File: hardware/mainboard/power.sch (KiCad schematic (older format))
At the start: 12 parts, among them U1 LM4040DBZ-10, U2 LM1117-3.3

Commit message: First pass layout & component selection for mainboard
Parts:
- C1, C4: footprint Capacitor_SMD:C_0805_2012Metric_Pad1.15x1.40mm_HandSolder -> Capacitor_SMD:C_0603_1608Metric_Pad1.05x0.95mm_HandSolder; finalized no -> yes
- D1, D2, FB1, FB2, FB3, U1: finalized no -> yes
- R1: footprint Resistor_SMD:R_1206_3216Metric_Pad1.42x1.75mm_HandSolder -> Resistor_SMD:R_0603_1608Metric_Pad1.05x0.95mm_HandSolder; Reqs (none) -> 1%; mpn ERA8AEB222V -> ERA-3AED222V
- U2: finalized no -> yes; mpn (none) -> LM1117IMP-3.3/NOPB
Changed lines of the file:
@@
 F 2 "Diode_SMD:D_SOD-123" H 2250 1100 50  0001 C CNN
 F 3 "~" H 2250 1100 50  0001 C CNN
-F 4 "no" H 2250 1100 50  0001 C CNN "finalized"
+F 4 "yes" H 2250 1100 50  0001 C CNN "finalized"
 F 5 "MF-DIO-SOD123-1N4148" H 2250 1100 50  0001 C CNN "mpn"
 	1    2250 1100
@@
 F 2 "Diode_SMD:D_SOD-123" H 2250 1600 50  0001 C CNN
 F 3 "~" H 2250 1600 50  0001 C CNN
-F 4 "no" H 2250 1600 50  0001 C CNN "finalized"
+F 4 "yes" H 2250 1600 50  0001 C CNN "finalized"
 F 5 "MF-DIO-SOD123-1N4148" H 2250 1600 50  0001 C CNN "mpn"
 	1    2250 1600
@@
 F 2 "Package_TO_SOT_SMD:SOT-223-3_TabPin2" H 4650 1200 50  0001 C CNN
 F 3 "http://www.ti.com/lit/ds/symlink/lm1117.pdf" H 4650 1200 50  0001 C CNN
-F 4 "no" H 4650 1200 50  0001 C CNN "finalized"
+F 4 "yes" H 4650 1200 50  0001 C CNN "finalized"
+F 5 "LM1117IMP-3.3/NOPB" H 4650 1200 50  0001 C CNN "mpn"
 	1    4650 1200
 	1    0    0    -1
@@
 F 0 "C4" H 5715 1396 50  0000 L CNN
 F 1 "0.1uF" H 5715 1305 50  0000 L CNN
-F 2 "Capacitor_SMD:C_0805_2012Metric_Pad1.15x1.40mm_HandSolder" H 5638 1200 50  0001 C CNN
+F 2 "Capacitor_SMD:C_0603_1608Metric_Pad1.05x0.95mm_HandSolder" H 5638 1200 50  0001 C CNN
 F 3 "~" H 5600 1350 50  0001 C CNN
-F 4 "no" H 5600 1350 50  0001 C CNN "finalized"
+F 4 "yes" H 5600 1350 50  0001 C CNN "finalized"
 F 5 "MF-CAP-0603-0.1uF" H 5600 1350 50  0001 C CNN "mpn"
 	1    5600 1350
@@
 F 3 "~" H 5950 1100 50  0001 C CNN
 F 4 "710-742792664" H 5950 1100 50  0001 C CNN "mpn"
-F 5 "no" H 5950 1100 50  0001 C CNN "finalized"
+F 5 "yes" H 5950 1100 50  0001 C CNN "finalized"
 	1    5950 1100
 	-1   0    0    1
@@
 F 3 "~" H 1800 1600 50  0001 C CNN
 F 4 "710-742792664" H 1800 1600 50  0001 C CNN "mpn"
-F 5 "no" H 1800 1600 50  0001 C CNN "finalized"
+F 5 "yes" H 1800 1600 50  0001 C CNN "finalized"
 	1    1800 1600
 	0    -1   -1   0
@@
 F 2 "Package_TO_SOT_SMD:SOT-23" H 2200 3100 50  0001 C CIN
 F 3 "http://www.ti.com/lit/ds/symlink/lm4040-n.pdf" H 2200 3300 50  0001 C CIN
-F 4 "no" H 2200 3300 50  0001 C CNN "finalized"
+F 4 "yes" H 2200 3300 50  0001 C CNN "finalized"
 F 5 "LM4040DIM3-10.0/NOPB" H 2200 3300 50  0001 C CNN "mpn"
 	1    2200 3300
@@
 F 0 "R1" H 2268 2846 50  0000 L CNN
 F 1 "2.2k" H 2268 2755 50  0000 L CNN
-F 2 "Resistor_SMD:R_1206_3216Metric_Pad1.42x1.75mm_HandSolder" V 2240 2790 50  0001 C CNN
+F 2 "Resistor_SMD:R_0603_1608Metric_Pad1.05x0.95mm_HandSolder" V 2240 2790 50  0001 C CNN
 F 3 "~" H 2200 2800 50  0001 C CNN
 F 4 "no" H 2200 2800 50  0001 C CNN "finalized"
-F 5 "ERA8AEB222V" H 2200 2800 50  0001 C CNN "mpn"
+F 5 "ERA-3AED222V" H 2200 2800 50  0001 C CNN "mpn"
+F 6 "1%" H 2200 2800 50  0001 C CNN "Reqs"
 	1    2200 2800
 	1    0    0    -1
@@
 F 0 "C1" H 2665 3346 50  0000 L CNN
 F 1 "0.1uF" H 2665 3255 50  0000 L CNN
-F 2 "Capacitor_SMD:C_0805_2012Metric_Pad1.15x1.40mm_HandSolder" H 2588 3150 50  0001 C CNN
+F 2 "Capacitor_SMD:C_0603_1608Metric_Pad1.05x0.95mm_HandSolder" H 2588 3150 50  0001 C CNN
 F 3 "~" H 2550 3300 50  0001 C CNN
-F 4 "no" H 2550 3300 50  0001 C CNN "finalized"
+F 4 "yes" H 2550 3300 50  0001 C CNN "finalized"
 F 5 "MF-CAP-0603-0.1uF" H 2550 3300 50  0001 C CNN "mpn"
 	1    2550 3300
@@
 F 3 "~" H 1800 1100 50  0001 C CNN
 F 4 "710-742792664" H 1800 1100 50  0001 C CNN "mpn"
-F 5 "no" H 1800 1100 50  0001 C CNN "finalized"
+F 5 "yes" H 1800 1100 50  0001 C CNN "finalized"
 	1    1800 1100
 	0    -1   -1   0

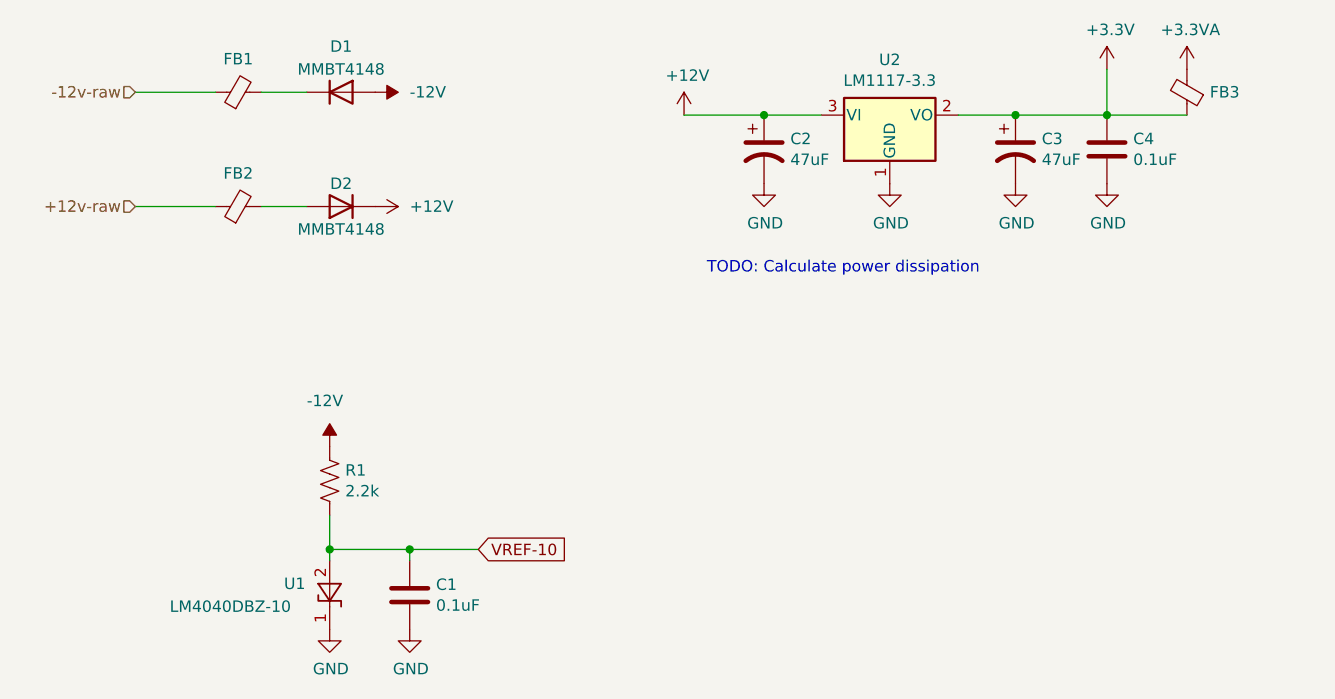
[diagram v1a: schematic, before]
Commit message: Refine mainboard even more - ground planes, caps, oh my!
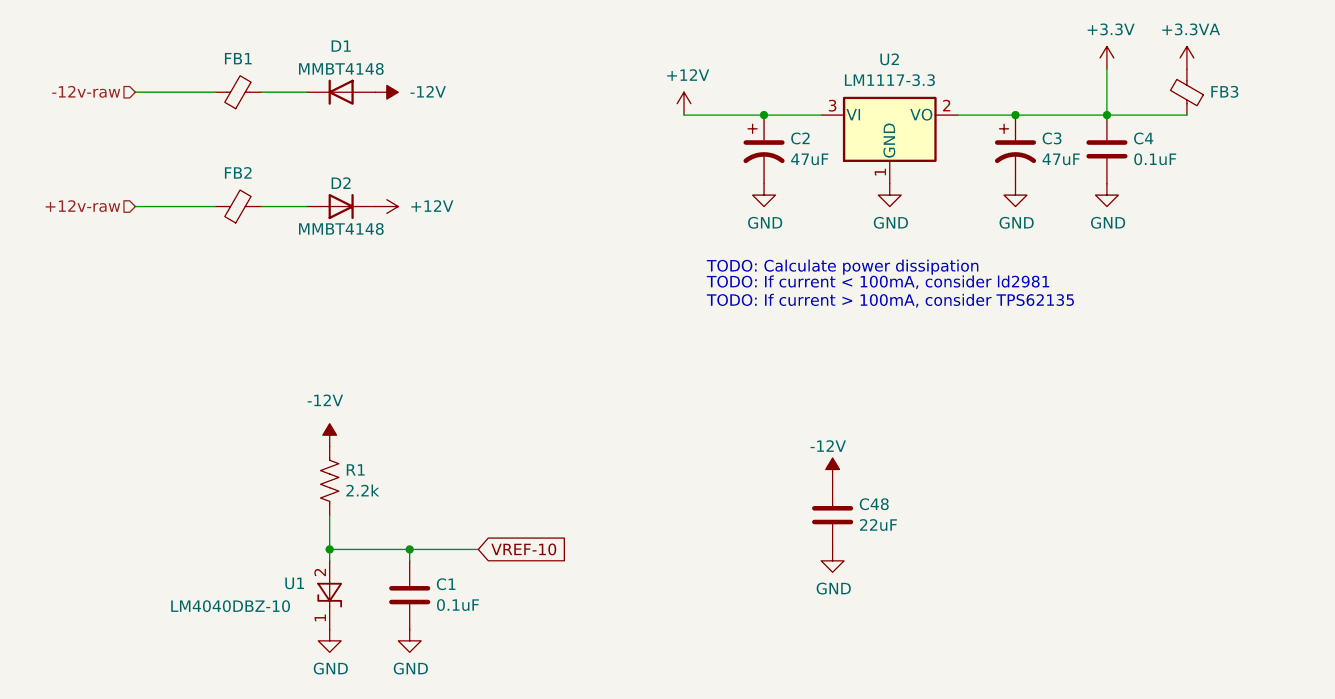
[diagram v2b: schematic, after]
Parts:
- added C48: 22uF, Capacitor_SMD:C_1210_3225Metric_Pad1.42x2.65mm_HandSolder, symbol Device:C
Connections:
- net -12V: now also C48.1
- net GND: now also C48.2
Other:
- note added: "TODO: If current < 100mA, consider ld2981\nTODO: If current > 100mA, consider TPS62135"
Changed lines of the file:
@@
 Wire Wire Line
 	1350 1100 1700 1100
+Text Notes 3850 2050 0    50   ~ 0
+TODO: If current < 100mA, consider ld2981\nTODO: If current > 100mA, consider TPS62135
+$Comp
+L power:GND #PWR02
+U 1 1 5F1FA7FD
+P 4400 3100
+F 0 "#PWR02" H 4400 2850 50  0001 C CNN
+F 1 "GND" H 4405 2927 50  0000 C CNN
+F 2 "" H 4400 3100 50  0001 C CNN
+F 3 "" H 4400 3100 50  0001 C CNN
+	1    4400 3100
+	1    0    0    -1
+$EndComp
+$Comp
+L Device:C C48
+U 1 1 5F1FB229
+P 4400 2950
+F 0 "C48" H 4515 2996 50  0000 L CNN
+F 1 "22uF" H 4515 2905 50  0000 L CNN
+F 2 "Capacitor_SMD:C_1210_3225Metric_Pad1.42x2.65mm_HandSolder" H 4438 2800 50  0001 C CNN
+F 3 "~" H 4400 2950 50  0001 C CNN
+F 4 "GRM32ER71E226ME15L" H 4400 2950 50  0001 C CNN "mpn"
+F 5 "yes" H 4400 2950 50  0001 C CNN "finalized"
+	1    4400 2950
+	1    0    0    -1
+$EndComp
+$Comp
+L power:-12V #PWR01
+U 1 1 5F200052
+P 4400 2800
+F 0 "#PWR01" H 4400 2900 50  0001 C CNN
+F 1 "-12V" H 4300 2950 50  0000 L CNN
+F 2 "" H 4400 2800 50  0001 C CNN
+F 3 "" H 4400 2800 50  0001 C CNN
+	1    4400 2800
+	1    0    0    -1
+$EndComp
 $EndSCHEMATC

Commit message: Fixup ERC errors
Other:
- moved on the sheet: D2, FB2
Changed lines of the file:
@@
 L Device:D D2
 U 1 1 5F079176
-P 2250 1600
-F 0 "D2" H 2250 1500 50  0000 C CNN
-F 1 "MMBT4148" H 2250 1700 50  0000 C CNN
-F 2 "Diode_SMD:D_SOD-123" H 2250 1600 50  0001 C CNN
-F 3 "~" H 2250 1600 50  0001 C CNN
-F 4 "yes" H 2250 1600 50  0001 C CNN "finalized"
-F 5 "MF-DIO-SOD123-1N4148" H 2250 1600 50  0001 C CNN "mpn"
-	1    2250 1600
+P 2250 1750
+F 0 "D2" H 2250 1550 50  0000 C CNN
+F 1 "MMBT4148" H 2250 1650 50  0000 C CNN
+F 2 "Diode_SMD:D_SOD-123" H 2250 1750 50  0001 C CNN
+F 3 "~" H 2250 1750 50  0001 C CNN
+F 4 "yes" H 2250 1750 50  0001 C CNN "finalized"
+F 5 "MF-DIO-SOD123-1N4148" H 2250 1750 50  0001 C CNN "mpn"
+	1    2250 1750
 	-1   0    0    1
 $EndComp
@@
 L power:+12V #PWR06
 U 1 1 5F07A8DF
-P 2400 1600
-F 0 "#PWR06" H 2400 1450 50  0001 C CNN
-F 1 "+12V" V 2400 1750 50  0000 L CNN
-F 2 "" H 2400 1600 50  0001 C CNN
-F 3 "" H 2400 1600 50  0001 C CNN
-	1    2400 1600
+P 2400 1750
+F 0 "#PWR06" H 2400 1600 50  0001 C CNN
+F 1 "+12V" V 2400 1900 50  0000 L CNN
+F 2 "" H 2400 1750 50  0001 C CNN
+F 3 "" H 2400 1750 50  0001 C CNN
+	1    2400 1750
 	0    1    1    0
 $EndComp
@@
 L Device:Ferrite_Bead_Small FB2
 U 1 1 5F08BA03
-P 1800 1600
-F 0 "FB2" V 1945 1600 50  0000 C CNN
-F 1 "Ferrite_Bead_Small" V 1946 1600 50  0001 C CNN
-F 2 "Inductor_SMD:L_0603_1608Metric_Pad1.05x0.95mm_HandSolder" V 1730 1600 50  0001 C CNN
-F 3 "~" H 1800 1600 50  0001 C CNN
-F 4 "710-742792664" H 1800 1600 50  0001 C CNN "mpn"
-F 5 "yes" H 1800 1600 50  0001 C CNN "finalized"
-	1    1800 1600
+P 1800 1750
+F 0 "FB2" V 1945 1750 50  0000 C CNN
+F 1 "Ferrite_Bead_Small" V 1946 1750 50  0001 C CNN
+F 2 "Inductor_SMD:L_0603_1608Metric_Pad1.05x0.95mm_HandSolder" V 1730 1750 50  0001 C CNN
+F 3 "~" H 1800 1750 50  0001 C CNN
+F 4 "710-742792664" H 1800 1750 50  0001 C CNN "mpn"
+F 5 "yes" H 1800 1750 50  0001 C CNN "finalized"
+	1    1800 1750
 	0    -1   -1   0
 $EndComp
@@
 	1900 1100 2100 1100
 Wire Wire Line
-	1900 1600 2100 1600
+	1900 1750 2100 1750
 Text Notes 3850 1900 0    50   ~ 0
 TODO: Calculate power dissipation
@@
 Text HLabel 1350 1100 0    50   Input ~ 0
 -12v-raw
-Text HLabel 1350 1600 0    50   Input ~ 0
+Text HLabel 1350 1750 0    50   Input ~ 0
 +12v-raw
 Wire Wire Line
-	1350 1600 1700 1600
+	1350 1750 1700 1750
 Wire Wire Line
 	1350 1100 1700 1100
@@
 	1    0    0    -1
 $EndComp
+$Comp
+L power:PWR_FLAG #FLG0101
+U 1 1 5F2346B6
+P 2400 1100
+F 0 "#FLG0101" H 2400 1175 50  0001 C CNN
+F 1 "PWR_FLAG" H 2400 1273 50  0000 C CNN
+F 2 "" H 2400 1100 50  0001 C CNN
+F 3 "~" H 2400 1100 50  0001 C CNN
+	1    2400 1100
+	-1   0    0    1
+$EndComp
+Connection ~ 2400 1100
+$Comp
+L power:PWR_FLAG #FLG0102
+U 1 1 5F2359DC
+P 2400 1750
+F 0 "#FLG0102" H 2400 1825 50  0001 C CNN
+F 1 "PWR_FLAG" H 2400 1923 50  0000 C CNN
+F 2 "" H 2400 1750 50  0001 C CNN
+F 3 "~" H 2400 1750 50  0001 C CNN
+	1    2400 1750
+	-1   0    0    1
+$EndComp
+Connection ~ 2400 1750
+$Comp
+L power:GND #PWR0143
+U 1 1 5F239B16
+P 1100 2250
+F 0 "#PWR0143" H 1100 2000 50  0001 C CNN
+F 1 "GND" H 1105 2077 50  0000 C CNN
+F 2 "" H 1100 2250 50  0001 C CNN
+F 3 "" H 1100 2250 50  0001 C CNN
+	1    1100 2250
+	1    0    0    -1
+$EndComp
+$Comp
+L power:PWR_FLAG #FLG0103
+U 1 1 5F23AB23
+P 1100 2250
+F 0 "#FLG0103" H 1100 2325 50  0001 C CNN
+F 1 "PWR_FLAG" H 1100 2423 50  0000 C CNN
+F 2 "" H 1100 2250 50  0001 C CNN
+F 3 "~" H 1100 2250 50  0001 C CNN
+	1    1100 2250
+	1    0    0    -1
+$EndComp
+$Comp
+L power:PWR_FLAG #FLG0104
+U 1 1 5F23BDA0
+P 5950 1000
+F 0 "#FLG0104" H 5950 1075 50  0001 C CNN
+F 1 "PWR_FLAG" V 5950 1128 50  0000 L CNN
+F 2 "" H 5950 1000 50  0001 C CNN
+F 3 "~" H 5950 1000 50  0001 C CNN
+	1    5950 1000
+	0    1    1    0
+$EndComp
+Connection ~ 5950 1000
 $EndSCHEMATC

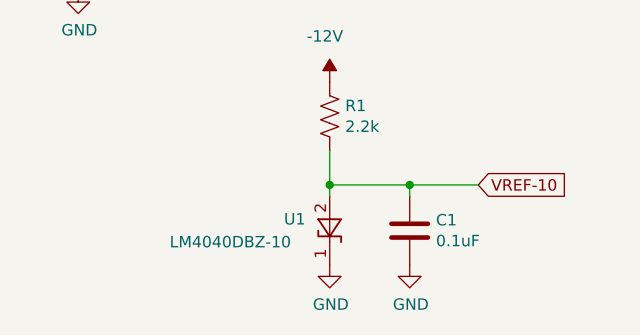
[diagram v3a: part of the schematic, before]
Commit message: Check passive ratings
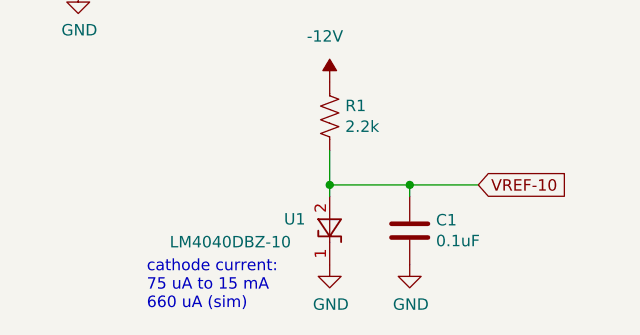
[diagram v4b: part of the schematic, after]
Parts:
- C1, C4: mpn specs (none) -> 10%, 25v
- C2: Reqs (none) -> ESR 0.3-22 Ohms, 16v+; mpn specs (none) -> 20%, 35v, 0.36 Ohms
- C3: Reqs ESR 0.3-22 Ohms -> ESR 0.3-22 Ohms, 16v+; mpn specs (none) -> 20%, 35v, 0.36 Ohms
- C48: mpn specs (none) -> 20% 25v
- FB1, FB2, FB3: mpn specs (none) -> 300mA, 600 mOhms DC, 1 kOhms AC
- R1: mpn specs (none) -> 100mW
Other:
- note added: "cathode current:\n75 uA to 15 mA\n660 uA (sim)\n"
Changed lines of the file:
@@
 F 2 "Capacitor_SMD:CP_Elec_6.3x5.8" H 5200 1350 50  0001 C CNN
 F 3 "~" H 5200 1350 50  0001 C CNN
-F 4 "ESR 0.3-22 Ohms" H 5200 1350 50  0001 C CNN "Reqs"
+F 4 "ESR 0.3-22 Ohms, 16v+" H 5200 1350 50  0001 C CNN "Reqs"
 F 5 "EEE-FK1V470P" H 5200 1350 50  0001 C CNN "mpn"
 F 6 "yes" H 5200 1350 50  0001 C CNN "finalized"
+F 7 "20%, 35v, 0.36 Ohms" H 5200 1350 50  0001 C CNN "mpn specs"
 	1    5200 1350
 	1    0    0    -1
@@
 F 4 "yes" H 5600 1350 50  0001 C CNN "finalized"
 F 5 "MF-CAP-0603-0.1uF" H 5600 1350 50  0001 C CNN "mpn"
+F 6 "10%, 25v" H 5600 1350 50  0001 C CNN "mpn specs"
 	1    5600 1350
 	1    0    0    -1
@@
 F 4 "710-742792664" H 5950 1100 50  0001 C CNN "mpn"
 F 5 "yes" H 5950 1100 50  0001 C CNN "finalized"
+F 6 "300mA, 600 mOhms DC, 1 kOhms AC" H 5950 1100 50  0001 C CNN "mpn specs"
 	1    5950 1100
 	-1   0    0    1
@@
 F 4 "EEE-FK1V470P" H 4100 1350 50  0001 C CNN "mpn"
 F 5 "yes" H 4100 1350 50  0001 C CNN "finalized"
+F 6 "ESR 0.3-22 Ohms, 16v+" H 4100 1350 50  0001 C CNN "Reqs"
+F 7 "20%, 35v, 0.36 Ohms" H 4100 1350 50  0001 C CNN "mpn specs"
 	1    4100 1350
 	1    0    0    -1
@@
 F 4 "710-742792664" H 1800 1750 50  0001 C CNN "mpn"
 F 5 "yes" H 1800 1750 50  0001 C CNN "finalized"
+F 6 "300mA, 600 mOhms DC, 1 kOhms AC" H 1800 1750 50  0001 C CNN "mpn specs"
 	1    1800 1750
 	0    -1   -1   0
@@
 F 5 "ERA-3AED222V" H 2200 2800 50  0001 C CNN "mpn"
 F 6 "1%" H 2200 2800 50  0001 C CNN "Reqs"
+F 7 "100mW" H 2200 2800 50  0001 C CNN "mpn specs"
 	1    2200 2800
 	1    0    0    -1
@@
 F 4 "yes" H 2550 3300 50  0001 C CNN "finalized"
 F 5 "MF-CAP-0603-0.1uF" H 2550 3300 50  0001 C CNN "mpn"
+F 6 "10%, 25v" H 2550 3300 50  0001 C CNN "mpn specs"
 	1    2550 3300
 	1    0    0    -1
@@
 F 4 "710-742792664" H 1800 1100 50  0001 C CNN "mpn"
 F 5 "yes" H 1800 1100 50  0001 C CNN "finalized"
+F 6 "300mA, 600 mOhms DC, 1 kOhms AC" H 1800 1100 50  0001 C CNN "mpn specs"
 	1    1800 1100
 	0    -1   -1   0
@@
 F 4 "GRM32ER71E226ME15L" H 4400 2950 50  0001 C CNN "mpn"
 F 5 "yes" H 4400 2950 50  0001 C CNN "finalized"
+F 6 "20% 25v" H 4400 2950 50  0001 C CNN "mpn specs"
 	1    4400 2950
 	1    0    0    -1
@@
 $EndComp
 Connection ~ 5950 1000
+Text Notes 1400 3650 0    50   ~ 0
+cathode current:\n75 uA to 15 mA\n660 uA (sim)\n
 $EndSCHEMATC

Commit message: Bumb schematics after generating gerbers and assigning alt mpns
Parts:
- C1, C4: mpn alt (none) -> GRM188R72A104KA35D
- C2, C3: mpn alt (none) -> EEE-FK1H470XP
- D1, D2: mpn alt (none) -> 1N4148W-7-F
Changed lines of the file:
@@
 F 4 "yes" H 2250 1100 50  0001 C CNN "finalized"
 F 5 "MF-DIO-SOD123-1N4148" H 2250 1100 50  0001 C CNN "mpn"
+F 6 "1N4148W-7-F" H 2250 1100 50  0001 C CNN "mpn alt"
 	1    2250 1100
 	1    0    0    -1
@@
 F 4 "yes" H 2250 1750 50  0001 C CNN "finalized"
 F 5 "MF-DIO-SOD123-1N4148" H 2250 1750 50  0001 C CNN "mpn"
+F 6 "1N4148W-7-F" H 2250 1750 50  0001 C CNN "mpn alt"
 	1    2250 1750
 	-1   0    0    1
@@
 F 6 "yes" H 5200 1350 50  0001 C CNN "finalized"
 F 7 "20%, 35v, 0.36 Ohms" H 5200 1350 50  0001 C CNN "mpn specs"
+F 8 "EEE-FK1H470XP" H 5200 1350 50  0001 C CNN "mpn alt"
 	1    5200 1350
 	1    0    0    -1
@@
 F 5 "MF-CAP-0603-0.1uF" H 5600 1350 50  0001 C CNN "mpn"
 F 6 "10%, 25v" H 5600 1350 50  0001 C CNN "mpn specs"
+F 7 "GRM188R72A104KA35D" H 5600 1350 50  0001 C CNN "mpn alt"
 	1    5600 1350
 	1    0    0    -1
@@
 F 6 "ESR 0.3-22 Ohms, 16v+" H 4100 1350 50  0001 C CNN "Reqs"
 F 7 "20%, 35v, 0.36 Ohms" H 4100 1350 50  0001 C CNN "mpn specs"
+F 8 "EEE-FK1H470XP" H 4100 1350 50  0001 C CNN "mpn alt"
 	1    4100 1350
 	1    0    0    -1
@@
 F 5 "MF-CAP-0603-0.1uF" H 2550 3300 50  0001 C CNN "mpn"
 F 6 "10%, 25v" H 2550 3300 50  0001 C CNN "mpn specs"
+F 7 "GRM188R72A104KA35D" H 2550 3300 50  0001 C CNN "mpn alt"
 	1    2550 3300
 	1    0    0    -1

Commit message: Fix a few more mpns
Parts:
- C1, C4: mpn alt GRM188R72A104KA35D -> GCM188R91E104KA37D
- C48: mpn GRM32ER71E226ME15L -> GRM32ER71E226ME15K; mpn specs 20% 25v -> 20% 25v, consider 0805 GRM21BR61E226ME44K
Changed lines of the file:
@@
 F 5 "MF-CAP-0603-0.1uF" H 5600 1350 50  0001 C CNN "mpn"
 F 6 "10%, 25v" H 5600 1350 50  0001 C CNN "mpn specs"
-F 7 "GRM188R72A104KA35D" H 5600 1350 50  0001 C CNN "mpn alt"
+F 7 "GCM188R91E104KA37D" H 5600 1350 50  0001 C CNN "mpn alt"
 	1    5600 1350
 	1    0    0    -1
@@
 F 5 "MF-CAP-0603-0.1uF" H 2550 3300 50  0001 C CNN "mpn"
 F 6 "10%, 25v" H 2550 3300 50  0001 C CNN "mpn specs"
-F 7 "GRM188R72A104KA35D" H 2550 3300 50  0001 C CNN "mpn alt"
+F 7 "GCM188R91E104KA37D" H 2550 3300 50  0001 C CNN "mpn alt"
 	1    2550 3300
 	1    0    0    -1
@@
 F 2 "Capacitor_SMD:C_1210_3225Metric_Pad1.42x2.65mm_HandSolder" H 4438 2800 50  0001 C CNN
 F 3 "~" H 4400 2950 50  0001 C CNN
-F 4 "GRM32ER71E226ME15L" H 4400 2950 50  0001 C CNN "mpn"
+F 4 "GRM32ER71E226ME15K" H 4400 2950 50  0001 C CNN "mpn"
 F 5 "yes" H 4400 2950 50  0001 C CNN "finalized"
-F 6 "20% 25v" H 4400 2950 50  0001 C CNN "mpn specs"
+F 6 "20% 25v, consider 0805 GRM21BR61E226ME44K" H 4400 2950 50  0001 C CNN "mpn specs"
 	1    4400 2950
 	1    0    0    -1

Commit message: Change footprint for 22uF cap to 0805 to use a cheaper MPN
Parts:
- C48: footprint Capacitor_SMD:C_1210_3225Metric_Pad1.42x2.65mm_HandSolder -> Capacitor_SMD:C_0805_2012Metric_Pad1.15x1.40mm_HandSolder; mpn GRM32ER71E226ME15K -> GRM21BR61E226ME44K; mpn specs 20% 25v, consider 0805 GRM21BR61E226ME44K -> 20% 25v
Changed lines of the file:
@@
 F 0 "C48" H 4515 2996 50  0000 L CNN
 F 1 "22uF" H 4515 2905 50  0000 L CNN
-F 2 "Capacitor_SMD:C_1210_3225Metric_Pad1.42x2.65mm_HandSolder" H 4438 2800 50  0001 C CNN
+F 2 "Capacitor_SMD:C_0805_2012Metric_Pad1.15x1.40mm_HandSolder" H 4438 2800 50  0001 C CNN
 F 3 "~" H 4400 2950 50  0001 C CNN
-F 4 "GRM32ER71E226ME15K" H 4400 2950 50  0001 C CNN "mpn"
+F 4 "GRM21BR61E226ME44K" H 4400 2950 50  0001 C CNN "mpn"
 F 5 "yes" H 4400 2950 50  0001 C CNN "finalized"
-F 6 "20% 25v, consider 0805 GRM21BR61E226ME44K" H 4400 2950 50  0001 C CNN "mpn specs"
+F 6 "20% 25v" H 4400 2950 50  0001 C CNN "mpn specs"
 	1    4400 2950
 	1    0    0    -1

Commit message: Change the RC differentiator capacitor to allow longer for discharging
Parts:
- R1: finalized no -> yes
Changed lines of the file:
@@
 F 2 "Resistor_SMD:R_0603_1608Metric_Pad1.05x0.95mm_HandSolder" V 2240 2790 50  0001 C CNN
 F 3 "~" H 2200 2800 50  0001 C CNN
-F 4 "no" H 2200 2800 50  0001 C CNN "finalized"
+F 4 "yes" H 2200 2800 50  0001 C CNN "finalized"
 F 5 "ERA-3AED222V" H 2200 2800 50  0001 C CNN "mpn"
 F 6 "1%" H 2200 2800 50  0001 C CNN "Reqs"
